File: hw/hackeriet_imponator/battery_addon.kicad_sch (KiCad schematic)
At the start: 6 parts

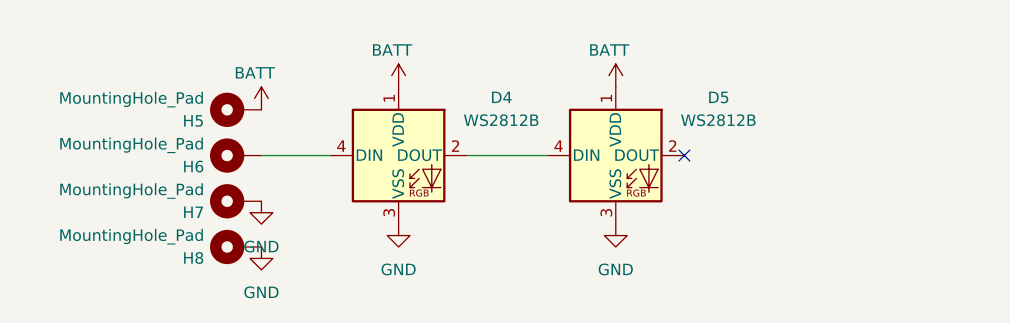
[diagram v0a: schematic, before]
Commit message: Major change. Resized PCB. Changed CPU. Added USB. Added headers. Added another layer for batteries
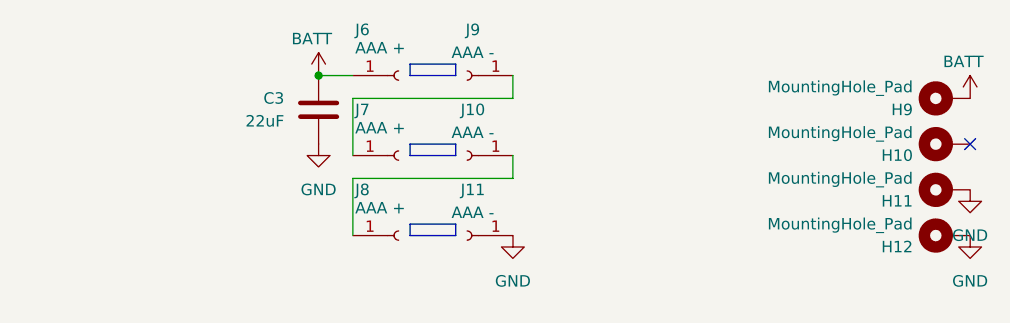
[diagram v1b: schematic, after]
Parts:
- removed D4, D5: WS2812B, LED_SMD:LED_WS2812B_PLCC4_5.0x5.0mm_P3.2mm, symbol LED:WS2812B
- removed H5, H6, H7, H8: MountingHole_Pad, MountingHole:MountingHole_2.5mm_Pad_TopBottom, symbol Mechanical:MountingHole_Pad
- added C3: 22uF, Capacitor_SMD:C_0603_1608Metric_Pad1.08x0.95mm_HandSolder, symbol Device:C
- added H10, H11, H12, H9: MountingHole_Pad, MountingHole:MountingHole_2.5mm_Pad_TopBottom, symbol Mechanical:MountingHole_Pad
- added J10, J11, J9: AAA -, imponator_footprint_lib:BAT_591, symbol Connector:Conn_01x01_Socket
- added J6, J7, J8: AAA +, imponator_footprint_lib:BAT_597, symbol Connector:Conn_01x01_Socket
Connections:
- net BATT: now also C3.2, H9.1, J6.1 (Pin_1)
- net GND: now also C3.1, H11.1, H12.1, J11.1 (Pin_1)
- new net: J7.1 (Pin_1), J9.1 (Pin_1)
- new net: J10.1 (Pin_1), J8.1 (Pin_1)
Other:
- title: Imponator, Outer Ring -> Imponator, Battery Addon (Optional)
